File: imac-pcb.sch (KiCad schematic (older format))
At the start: 18 parts, among them P1 PROBE1, P2 PROBE2, P3 INPUTS, U1 DG2525

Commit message: schematic changes & moved datasheet files
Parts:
- removed P?: PIEZO_IN, symbol SCREW_TERMINAL_X2
- added J?: PIEZO_IN, symbol JACK_3P
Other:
- note added: "All incoming signals are made to ride on a 2.5V reference voltage."
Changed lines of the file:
@@
-$EndComp
-$Comp
-L SCREW_TERMINAL_X2 P?
-U 1 1 585BAACF
-P 1700 5700
-F 0 "P?" H 1700 5850 50  0000 C CNN
-F 1 "PIEZO_IN" V 1925 5675 50  0000 C CNN
-F 2 "" H 1600 5650 50  0000 C CNN
-F 3 "" H 1600 5650 50  0000 C CNN
-	1    1700 5700
-	-1   0    0    1
 $EndComp
 $Comp
@@
 Text Notes 4325 3650 2    47   ~ 0
 Buffer, Attenuation, and Bias?
+$Comp
+L JACK_3P J?
+U 1 1 58611DEF
+P 1500 5725
+F 0 "J?" H 1200 5475 60  0000 C CNN
+F 1 "PIEZO_IN" H 1350 5975 60  0000 C CNN
+F 2 "" H 1450 5725 60  0000 C CNN
+F 3 "" H 1450 5725 60  0000 C CNN
+	1    1500 5725
+	1    0    0    -1
+$EndComp
+Text Notes 1225 4500 0    60   ~ 0
+All incoming signals are made to ride on a 2.5V reference voltage.
 $EndSCHEMATC

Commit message: small schematic updates
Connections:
- net labels added: AUDIO_OUTA, AUDIO_OUTB, EXT_IN1, EXT_IN2, EXT_OUT, LED_CTRL1, LED_CTRL2
- net labels removed: COIL, CTRL_LED1, CTRL_LED2, OUTA, OUTA_LOW_Z, OUTB, OUTB_LOW_Z, PIEZO
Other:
- moved on the sheet: P3, P?
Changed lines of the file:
@@
 L ARDUINO_MICRO P?
 U 1 1 585B9FD9
-P 8700 2275
-F 0 "P?" H 8700 3175 50  0000 C CNN
-F 1 "ARDUINO_MICRO" V 8700 2275 50  0000 C CNN
-F 2 "" H 8700 1175 50  0000 C CNN
-F 3 "" H 8700 1175 50  0000 C CNN
-	1    8700 2275
+P 10375 1625
+F 0 "P?" H 10375 2525 50  0000 C CNN
+F 1 "ARDUINO_MICRO" V 10375 1625 50  0000 C CNN
+F 2 "" H 10375 525 50  0000 C CNN
+F 3 "" H 10375 525 50  0000 C CNN
+	1    10375 1625
 	1    0    0    -1
 $EndComp
@@
 L CONN_01X05 P3
 U 1 1 585C5766
-P 3500 1800
-F 0 "P3" H 3500 2100 50  0000 C CNN
-F 1 "INPUTS" V 3600 1800 50  0000 C CNN
-F 2 "" H 3500 1800 50  0000 C CNN
-F 3 "" H 3500 1800 50  0000 C CNN
-	1    3500 1800
+P 3300 1800
+F 0 "P3" H 3300 2100 50  0000 C CNN
+F 1 "INPUTS" V 3400 1800 50  0000 C CNN
+F 2 "" H 3300 1800 50  0000 C CNN
+F 3 "" H 3300 1800 50  0000 C CNN
+	1    3300 1800
 	1    0    0    -1
 $EndComp
@@
 Text Label 9900 4550 2    47   ~ 0
 12V_RAW
-Text Label 3150 1600 2    47   ~ 0
+Text Label 2950 1600 2    47   ~ 0
 IN1
-Text Label 3150 1700 2    47   ~ 0
+Text Label 2950 1700 2    47   ~ 0
 IN2
-Text Label 3150 1800 2    47   ~ 0
+Text Label 2950 1800 2    47   ~ 0
 IN3
-Text Label 3150 1900 2    47   ~ 0
+Text Label 2950 1900 2    47   ~ 0
 IN4
-Text Label 3150 2000 2    47   ~ 0
+Text Label 2950 2000 2    47   ~ 0
 IN5
 $Comp
@@
 PB2
 Text Label 3850 1650 2    47   ~ 0
-PIEZO
+EXT_IN1
 Text Label 3850 1750 2    47   ~ 0
-COIL
+EXT_IN2
 $Comp
 L GND #PWR?
@@
 $EndComp
 Text Label 4550 950  0    47   ~ 0
-OUTA
-Text Label 4550 1350 0    47   ~ 0
-OUTB
-Text Label 4550 1750 0    47   ~ 0
-CTRL_LED1
-Text Label 4550 1850 0    47   ~ 0
-CTRL_LED2
+AUDIO_OUTA
 Text Label 4550 1250 0    47   ~ 0
-OUTA_LOW_Z
+AUDIO_OUTB
+Text Label 4550 1550 0    47   ~ 0
+LED_CTRL1
 Text Label 4550 1650 0    47   ~ 0
-OUTB_LOW_Z
+LED_CTRL2
 $Comp
 L GND #PWR?
@@
 	9900 4550 10100 4550
 Wire Wire Line
-	3150 2000 3300 2000
-Wire Wire Line
-	3150 1900 3300 1900
-Wire Wire Line
-	3150 1800 3300 1800
-Wire Wire Line
-	3150 1700 3300 1700
-Wire Wire Line
-	3150 1600 3300 1600
+	2950 2000 3100 2000
+Wire Wire Line
+	2950 1900 3100 1900
+Wire Wire Line
+	2950 1800 3100 1800
+Wire Wire Line
+	2950 1700 3100 1700
+Wire Wire Line
+	2950 1600 3100 1600
 Wire Wire Line
 	2900 900  2900 1050
@@
 Connection ~ 4450 1050
 Wire Wire Line
-	4300 1250 4550 1250
-Wire Wire Line
-	4300 1350 4550 1350
-Wire Wire Line
-	4300 1450 4450 1450
-Wire Wire Line
-	4450 1350 4450 1550
-Connection ~ 4450 1350
-Wire Wire Line
-	4450 1550 4300 1550
-Connection ~ 4450 1450
-Wire Wire Line
-	4300 1650 4550 1650
-Wire Wire Line
-	4300 1750 4550 1750
-Wire Wire Line
-	4300 1850 4550 1850
-Wire Wire Line
 	4300 2050 4500 2050
 Wire Wire Line
-	4500 1950 4500 2250
+	4500 1850 4500 2250
 Wire Wire Line
 	4300 1950 4500 1950
@@
 Text Notes 1225 4500 0    60   ~ 0
 All incoming signals are made to ride on a 2.5V reference voltage.
+Wire Wire Line
+	4300 1250 4550 1250
+Wire Wire Line
+	4450 1250 4450 1450
+Wire Wire Line
+	4450 1350 4300 1350
+Wire Wire Line
+	4450 1450 4300 1450
+Connection ~ 4450 1350
+Connection ~ 4450 1250
+Wire Wire Line
+	4300 1550 4550 1550
+Wire Wire Line
+	4300 1650 4550 1650
+Text Label 4550 1750 0    47   ~ 0
+EXT_OUT
+Wire Wire Line
+	4550 1750 4300 1750
+Wire Wire Line
+	4500 1850 4300 1850
+Connection ~ 4500 1950
 $EndSCHEMATC

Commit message: continued work on schematics
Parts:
- removed J?: STEREO_OUT2, symbol JACK_3P
- removed J?: PIEZO_IN, symbol JACK_3P
- removed P?: MOD_OUT_L, symbol SCREW_TERMINAL_X2
- removed P?: MOD_OUT_R, symbol SCREW_TERMINAL_X2
- removed P?: PATCHBAY_B, symbol CONN_03X06
- removed R?: 10, symbol R_Small
- removed U1: DG2525, symbol DG2525
- added 10n?, C?: 10n, symbol C_Small
- added C? (x5): 1u, symbol C_Small
- added C?: 220p*, symbol C_Small
- added C? (x2): 68n, symbol C_Small
- added C? (x2): 1u, symbol C
- added D?: 1N4148, symbol D
- added R?: 1meg, symbol R
- added R?: 50k, symbol R
- added R? (x3): 100, symbol R
- added R?: 100_OPT, symbol R_Small
- added R?: 100*, symbol R_Small
- added R?: 3.3k, symbol R
- added R?: 1k, symbol R
- added R?: R, symbol R
- added R?: 33k, symbol R
- added R? (x2): 220, symbol R
- added RV? (x4): 100k, symbol POT
- added RV?: 100k**, symbol POT
- added RV? (x2): 100k, symbol DUAL_POT
- added U? (x6): MCP6004, symbol MCP6004
- added U?: ADG849, symbol ADG849
- added U?: NCP4620, TO_SOT_Packages_SMD:SOT-23-5, symbol NCP4620
- J?: value STEREO_OUT1 -> STEREO_OUT
- J?: value COIL_IN -> EXT_IN
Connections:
- net labels added: +2V5, +5V, AUDIOA_OUT, AUDIOA_SEND, AUDIOB_OUT, AUDIOB_SEND, EXT_IN, MOD_CTRL, MOD_OUT, V+, VREF
- net labels removed: AUDIO_OUTA, AUDIO_OUTB, EXT_IN1, EXT_IN2, MODA_CTRL, MODA_SIG, MODB_CTRL, MODB_SIG, SWB_COM, SWB_CTRL, SWB_NC, SWB_NO
- wire segments 59 -> 146
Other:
- note added: "* Resistors are optional. Can be connected with a solder bridge.\n** Trimmer can be swapped for 1meg for higher input impedance"
- note added: "<--- make this into solder points instead?"
- note added: "AUDIO OUTPUTS\n"
- note added: "EXT INPUT CONDITIONING"
- note added: "Ext input has adjustable input attentuation and surge protection.\nThe resulting signal rides on the 2.5V reference voltage."
- note added: "MODULATION"
- note added: "TODO:\n* Power Regulation\n* LED Drivers"
- note removed: "All incoming signals are made to ride on a 2.5V reference voltage."
- note removed: "Buffer, Attenuation, and Bias?"
- note removed: "Channel Panning, Volume, and Filter"
- note removed: "Input circuit for Coil & Piezo"
- moved on the sheet: J?, P?

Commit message: bom updates
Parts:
- Q?: value STD30NF06L -> NX3008N***
- R?: value 100_OPT -> 100*
- R?: value 100* -> 100***
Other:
- note added: "* Resistors are optional. Can be connected with a solder bridge.\n** Trimmer can be swapped for 1meg for higher input impedance\n*** Replace/Experiment with BC817, and larger base/gate resistors"
- note removed: "* Resistors are optional. Can be connected with a solder bridge.\n** Trimmer can be swapped for 1meg for higher input impedance"
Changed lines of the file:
@@
 P 10450 4875
 F 0 "Q?" H 10750 4925 50  0000 R CNN
-F 1 "STD30NF06L" H 11100 4825 50  0000 R CNN
+F 1 "NX3008N***" H 11075 4825 50  0000 R CNN
 F 2 "" H 10650 4975 50  0000 C CNN
 F 3 "" H 10450 4875 50  0000 C CNN
@@
 U 1 1 5865864C
 P 8200 4775
-F 0 "C?" H 8210 4845 50  0000 L CNN
-F 1 "1u" H 8210 4695 50  0000 L CNN
+F 0 "C?" V 8050 4725 50  0000 L CNN
+F 1 "1u" V 8325 4725 50  0000 L CNN
 F 2 "" H 8200 4775 50  0000 C CNN
 F 3 "" H 8200 4775 50  0000 C CNN
@@
 P 10550 4525
 F 0 "R?" H 10580 4545 50  0000 L CNN
-F 1 "100_OPT" H 10580 4485 50  0000 L CNN
+F 1 "100*" H 10580 4485 50  0000 L CNN
 F 2 "" H 10550 4525 50  0000 C CNN
 F 3 "" H 10550 4525 50  0000 C CNN
@@
 $EndComp
 Text Notes 7050 6300 0    79   ~ 0
-* Resistors are optional. Can be connected with a solder bridge.\n** Trimmer can be swapped for 1meg for higher input impedance
+* Resistors are optional. Can be connected with a solder bridge.\n** Trimmer can be swapped for 1meg for higher input impedance\n*** Replace/Experiment with BC817, and larger base/gate resistors
 $Comp
 L R_Small R?
 U 1 1 5865E840
 P 10050 4875
-F 0 "R?" H 10080 4895 50  0000 L CNN
-F 1 "100*" H 10080 4835 50  0000 L CNN
+F 0 "R?" V 9950 4850 50  0000 L CNN
+F 1 "100***" V 10150 4800 50  0000 L CNN
 F 2 "" H 10050 4875 50  0000 C CNN
 F 3 "" H 10050 4875 50  0000 C CNN

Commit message: added led drivers, voltage selector, power conditioning to the schematic
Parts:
- removed P?: POWER_TERMINAL_X3, symbol POWER_TERMINAL_X3
- removed Q?: NX3008N***, symbol STD30NF06L
- added D?: LOW_POW_LED, symbol Led_Small
- added D? (x2): CLP6B-WKW, symbol CLP6B-WKW
- added P?: PWR_X3, symbol PWR_X3
- added Q?: PMV48XP, symbol PMV48XP
- added Q? (x3): NX3008N***, symbol NX3008N
- added R?: R_Small, symbol R_Small
- added R? (x2): 27, symbol R
- added R? (x2): 100***, symbol R_Small
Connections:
- net labels added: +12V_IN, +2V5_REF, +5V_IN, +5V_SYS
- net labels removed: +2V5, 12V_RAW, 5V_RAW
- wire segments 146 -> 218
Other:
- note added: "2.5V Reference"
- note added: "<--- make this into \nsolder points instead?"
- note added: "EXTERNAL INPUT"
- note added: "PATCHBAYS"
- note added: "POWER"
- note added: "SIGNAL \nMODULATION"
- note added: "TODO:\n* Arduino Connections to pads\n* Bypass caps\n* Power switch\n* Power led"
- note added: "This circuit uses the NCP1117-5 LDO regulator on the Arduino Micro for power regulation.\nThe circuit can be supplied with a 12V supply from the iMac's power supply. \nOr directly by the iMac's regulated 5V supply.\nThe Arduino's Vin pin has a 10k resistor to ground in order\nto keep the gate of this mosfet at 0 when no 12V supply is\nconnected."
- note added: "Voltage selector"
- note removed: "<--- make this into solder points instead?"
- note removed: "EXT INPUT CONDITIONING"
- note removed: "MODULATION"
- note removed: "Power Conditioning\n"
- note removed: "TODO:\n* Power Regulation\n* LED Drivers"
- moved on the sheet: C?, D?, J?, P1, P2, P3, P?, R?, RV?, U?, U?A

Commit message: begin work on pcb layout
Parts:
- removed D?: LOW_POW_LED, symbol Led_Small
- removed J?: PEDAL_IN, symbol JACK_3P
- added C9: 220u, Capacitors_SMD:c_elec_6.3x7.7, symbol CP
- added D2: KP-2012LSGC, LEDs:LED_0805, symbol KP-2012LSGC
- added P4: EXT_OUT, symbol CONN_01X02
- added RV6, RV7: 100k†, symbol BOURNS_TRIM
- C1, C10, C11, C12, C13, C2, C3, C4, C6, C7, C8: renamed from C?; footprint (none) -> Capacitors_SMD:C_0805
- C5: renamed from 10n?; footprint (none) -> Capacitors_SMD:C_0805
- D1: renamed from D?; footprint (none) -> Imac:SOD-323F
- D3, D4: renamed from D?; footprint (none) -> Imac:PLCC6-3in1-SMD-LED
- J1, J2: renamed from J?; footprint (none) -> Lumberg:Lumberg_1503_03
- P2: renamed from P?; footprint (none) -> Socket_Strips:Socket_Strip_Straight_2x12
- P5: renamed from P3; footprint (none) -> Socket_Strips:Socket_Strip_Angled_1x05
- P7: renamed from P?; footprint (none) -> Terminal_Blocks:TerminalBlock_Pheonix_MPT-2.54mm_3pol
- Q1, Q3, Q4: renamed from Q?; footprint (none) -> TO_SOT_Packages_SMD:SC-70
- Q2: renamed from Q?; footprint (none) -> TO_SOT_Packages_SMD:SOT-23
- R1, R14, R16, R3, R4, R5, R7, R8: renamed from R?; footprint (none) -> Resistors_SMD:R_0603
- R10: renamed from R?; value R_Small -> 1k5; footprint (none) -> Resistors_SMD:R_0603
- R11, R13: renamed from R?; footprint (none) -> Resistors_SMD:R_1812
- R12, R17, R18, R9: renamed from R?; footprint (none) -> Resistors_SMD:R_0603_HandSoldering
- R15: renamed from R?; value 50k -> 3k3; footprint (none) -> Resistors_SMD:R_0603
- R2: renamed from R?; value R -> 100**; footprint (none) -> Resistors_SMD:R_0603_HandSoldering
- R6: renamed from R?; value 3.3k -> 3k3; footprint (none) -> Resistors_SMD:R_0603
- U1, U2: renamed from U?; footprint (none) -> Housings_SOIC:SOIC-14_3.9x8.7mm_Pitch1.27mm
- U3: renamed from U?; footprint TO_SOT_Packages_SMD:SOT-23-5 -> TO_SOT_Packages_SMD:SC-70-5
- U4: renamed from U?; footprint (none) -> TO_SOT_Packages_SMD:SC-70-6
- gave numbers to parts that had none: 9
- renumbered P2 to P3
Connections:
- net AUDIOA_OUT is gone; now on net AUDIOA_SEND: RV1.1
- net AUDIOB_OUT is gone; now on net AUDIOB_SEND: RV2.1
- net V+ is gone; now on net 5V_SYS: R15.1, U2.4 (V+)
- net VREF is gone; now on net 2V5_REF: R14.2
- net EXT_OUT: now also P4.2 (P2)
- net GND: now also C9.2, D2.1 (K), P4.1 (P1), RV6.3, RV7.3; no longer P2.18 (P18), P2.19 (P19), P2.20 (P20)
- net D6: now reaches P8.11 (6p_A7)
- net D6: now also P2.20 (P20)
- net A0_IN: now reaches P8.21 (A0)
- net A0_IN: now also P2.19 (P19)
- net A1_IN: now reaches P8.22 (A1)
- net A1_IN: now also RV6.2
- net A2_IN: now reaches P8.23 (A2)
- net A2_IN: now also RV7.2
- net D3: now reaches P8.8 (3p_SCL)
- net D3: now also P2.18 (P18)
- net at C12.1, R14.1: now also U2.5 (+); no longer U2.3 (+)
- net at C4.1, R4.1: now also U1.10 (+); no longer U1.5 (+)
- net at C2.1, C7.2: now also U1.8, U1.9 (-); no longer U1.6 (-), U1.7
- net at RV2.2: now also U1.5 (+); no longer U1.3 (+)
- net at C5.1, R5.1: now also U1.12 (+); no longer U1.3 (+)
- net at C3.1, C8.2: now also U1.13 (-), U1.14; no longer U1.1, U1.2 (-)
- net at R10.2: now also D2.2 (A)
- net +12V renamed 12V_IN
- net +2V5 renamed 2V5_REF
- net +5V renamed 5V_SYS
- net 5V_SYS: now also C9.1, RV6.1, RV7.1; no longer P7.3 (+5V), Q2.3 (D)
- new net: C13.2, U2.6 (-), U2.7
- new net: RV4.6, U1.6 (-), U1.7
- new net 5V_IN: P7.3 (+5V), Q2.3 (D)
- no-connect marks 0 -> 23
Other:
- note added: "Ext input has adjustable input attentuation and \nsurge protection. The resulting signal rides on \nthe 2.5V reference voltage."
- note added: "† optional pots, solder pads available \nfor external connections (footpedal)"
- note removed: "<--- make this into \nsolder points instead?"
- note removed: "Ext input has adjustable input attentuation and surge protection.\nThe resulting signal rides on the 2.5V reference voltage."
- note removed: "TODO:\n* Arduino Connections to pads\n* Bypass caps\n* Power switch\n* Power led"
- moved on the sheet: C2, C3, P5

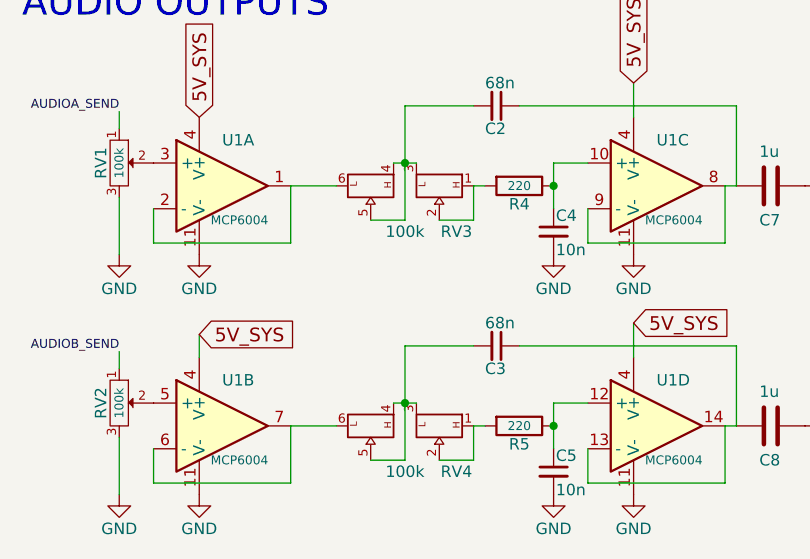
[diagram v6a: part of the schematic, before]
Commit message: begin layout of pcb
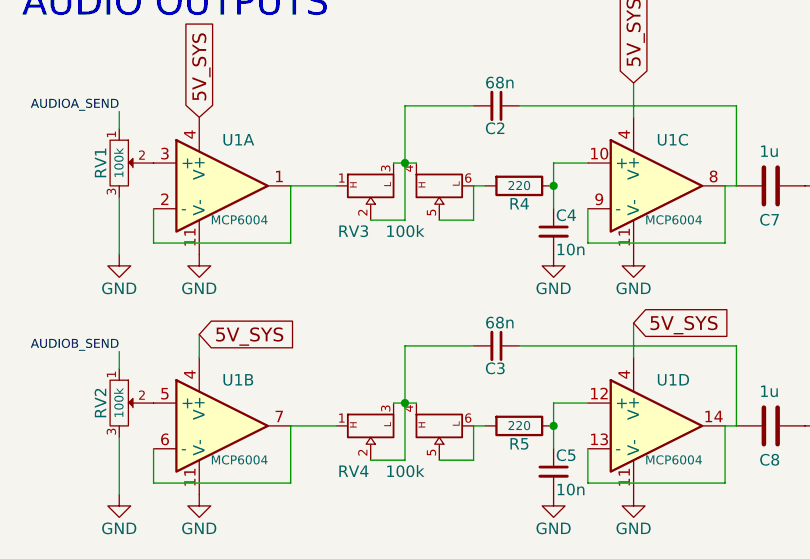
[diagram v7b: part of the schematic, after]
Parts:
- P1, P3: footprint (none) -> Imac:PSG01546_RCA_Phono_Connector
- P4: footprint (none) -> Imac:TerminalBlock_TE_282834-2-2.54mm_2pol
- P6: footprint (none) -> Imac:Socket_Strip_Straight_3x06
- P7: footprint Terminal_Blocks:TerminalBlock_Pheonix_MPT-2.54mm_3pol -> Imac:TerminalBlock_TE_282834-3-2.54mm_3pol
- P8: footprint (none) -> Imac:Arduino_Micro_2x1x17
- RV1, RV2, RV8, RV9: footprint (none) -> Imac:Pot_Bourns_PTV09A-4_Horizontal_Rear_mount
- RV3, RV4: footprint (none) -> Imac:Dual_Pot_Bourns_3301H-00X
- RV5: footprint (none) -> Imac:Trimpot_Bourns_3386F_Vishay_M63
- RV6, RV7: footprint (none) -> Imac:Trimpot_Bourns_Big_Pads_3386F_Vishay_M63
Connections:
- net at U1.1, U1.2 (-): now also RV3.1; no longer RV3.6
- net at C2.2, RV3.3, RV3.4: now also RV3.2; no longer RV3.5
- net at U1.6 (-), U1.7: now also RV4.1; no longer RV4.6
- net at C3.2, RV4.3, RV4.4: now also RV4.2; no longer RV4.5
- new net: R4.2, RV3.5, RV3.6
- new net: R5.2, RV4.5, RV4.6
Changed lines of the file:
@@
 F 0 "P8" H 9100 2550 50  0000 C CNN
 F 1 "ARDUINO_MICRO" V 9100 1650 50  0000 C CNN
-F 2 "" H 9100 550 50  0001 C CNN
+F 2 "Imac:Arduino_Micro_2x1x17" H 9100 550 50  0001 C CNN
 F 3 "" H 9100 550 50  0000 C CNN
 	1    9100 1650
@@
 F 0 "P1" H 960 4520 50  0000 C CNN
 F 1 "PROBE1" V 1060 4340 50  0000 C CNN
-F 2 "" H 950 4400 50  0001 C CNN
+F 2 "Imac:PSG01546_RCA_Phono_Connector" H 950 4400 50  0001 C CNN
 F 3 "" H 950 4400 50  0000 C CNN
 	1    950  4400
@@
 F 0 "P3" H 1560 4520 50  0000 C CNN
 F 1 "PROBE2" V 1660 4340 50  0000 C CNN
-F 2 "" H 1550 4400 50  0001 C CNN
+F 2 "Imac:PSG01546_RCA_Phono_Connector" H 1550 4400 50  0001 C CNN
 F 3 "" H 1550 4400 50  0000 C CNN
 	1    1550 4400
@@
 F 0 "P6" H 2200 1400 50  0000 C CNN
 F 1 "PATCHBAY_A" H 2200 700 50  0000 C CNN
-F 2 "" H 2200 1100 50  0001 C CNN
+F 2 "Imac:Socket_Strip_Straight_3x06" H 2200 1100 50  0001 C CNN
 F 3 "" H 2200 1100 50  0000 C CNN
 	1    2200 1100
@@
 F 0 "RV8" H 8050 4670 50  0000 C CNN
 F 1 "100k" H 8050 4750 39  0000 C CNN
-F 2 "" H 8050 4750 50  0001 C CNN
+F 2 "Imac:Pot_Bourns_PTV09A-4_Horizontal_Rear_mount" H 8050 4750 50  0001 C CNN
 F 3 "" H 8050 4750 50  0000 C CNN
 	1    8050 4750
@@
 F 0 "RV9" H 9950 4970 50  0000 C CNN
 F 1 "100k" H 9950 5050 39  0000 C CNN
-F 2 "" H 9950 5050 50  0001 C CNN
+F 2 "Imac:Pot_Bourns_PTV09A-4_Horizontal_Rear_mount" H 9950 5050 50  0001 C CNN
 F 3 "" H 9950 5050 50  0000 C CNN
 	1    9950 5050
@@
 F 0 "RV5" H 2500 3670 50  0000 C CNN
 F 1 "100k**" H 2500 3750 39  0000 C CNN
-F 2 "" H 2500 3750 50  0001 C CNN
+F 2 "Imac:Trimpot_Bourns_3386F_Vishay_M63" H 2500 3750 50  0001 C CNN
 F 3 "" H 2500 3750 50  0000 C CNN
 	1    2500 3750
@@
 F 0 "RV1" H 1050 5970 50  0000 C CNN
 F 1 "100k" H 1050 6050 39  0000 C CNN
-F 2 "" H 1050 6050 50  0001 C CNN
+F 2 "Imac:Pot_Bourns_PTV09A-4_Horizontal_Rear_mount" H 1050 6050 50  0001 C CNN
 F 3 "" H 1050 6050 50  0000 C CNN
 	1    1050 6050
@@
 F 0 "RV3" V 2500 6375 50  0000 C CNN
 F 1 "100k" V 2500 6150 50  0000 C CNN
-F 2 "" H 2300 6150 50  0001 C CNN
+F 2 "Imac:Dual_Pot_Bourns_3301H-00X" H 2300 6150 50  0001 C CNN
 F 3 "" H 2300 6150 50  0000 C CNN
 	1    2300 6150
-	0    1    1    0
+	0    -1   1    0
 $EndComp
 $Comp
@@
 F 0 "RV2" H 1050 7020 50  0000 C CNN
 F 1 "100k" H 1050 7100 39  0000 C CNN
-F 2 "" H 1050 7100 50  0001 C CNN
+F 2 "Imac:Pot_Bourns_PTV09A-4_Horizontal_Rear_mount" H 1050 7100 50  0001 C CNN
 F 3 "" H 1050 7100 50  0000 C CNN
 	1    1050 7100
@@
 F 0 "RV4" V 2500 7425 50  0000 C CNN
 F 1 "100k" V 2500 7200 50  0000 C CNN
-F 2 "" H 2300 7200 50  0001 C CNN
+F 2 "Imac:Dual_Pot_Bourns_3301H-00X" H 2300 7200 50  0001 C CNN
 F 3 "" H 2300 7200 50  0000 C CNN
 	1    2300 7200
-	0    1    1    0
+	0    -1   1    0
 $EndComp
 $Comp
@@
 F 0 "P7" H 5100 1800 50  0000 C CNN
 F 1 "PWR_X3" V 5325 1600 50  0000 C CNN
-F 2 "Terminal_Blocks:TerminalBlock_Pheonix_MPT-2.54mm_3pol" H 5000 1600 50  0001 C CNN
+F 2 "Imac:TerminalBlock_TE_282834-3-2.54mm_3pol" H 5000 1600 50  0001 C CNN
 F 3 "" H 5000 1600 50  0000 C CNN
 	1    5100 1600
@@
 F 0 "RV6" H 3050 1870 50  0000 C CNN
 F 1 "100k†" H 3050 1950 39  0000 C CNN
-F 2 "" H 3050 1950 50  0001 C CNN
+F 2 "Imac:Trimpot_Bourns_Big_Pads_3386F_Vishay_M63" H 3050 1950 50  0001 C CNN
 F 3 "" H 3050 1950 50  0000 C CNN
 	1    3050 1950
@@
 F 0 "RV7" H 3600 1870 50  0000 C CNN
 F 1 "100k†" H 3600 1950 39  0000 C CNN
-F 2 "" H 3600 1950 50  0001 C CNN
+F 2 "Imac:Trimpot_Bourns_Big_Pads_3386F_Vishay_M63" H 3600 1950 50  0001 C CNN
 F 3 "" H 3600 1950 50  0000 C CNN
 	1    3600 1950
@@
 F 0 "P4" H 2025 2050 50  0000 C CNN
 F 1 "EXT_OUT" V 2125 1900 50  0000 C CNN
-F 2 "" H 2025 1900 50  0001 C CNN
+F 2 "Imac:TerminalBlock_TE_282834-2-2.54mm_2pol" H 2025 1900 50  0001 C CNN
 F 3 "" H 2025 1900 50  0000 C CNN
 	1    2025 1900
